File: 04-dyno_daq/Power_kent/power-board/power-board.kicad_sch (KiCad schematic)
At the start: 0 parts

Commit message: done with inputs, working on power conversion
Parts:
- added C1: 100uF, symbol Device:C
- added C2: 1uF, symbol Device:C
- added D1: D_TVS, symbol Device:D_TVS
- added F1: Polyfuse, symbol Device:Polyfuse
- added J1: USB_C_Receptacle_PowerOnly_24P, symbol Connector:USB_C_Receptacle_PowerOnly_24P
- added J2_(placeholder): Conn_01x02, symbol Connector_Generic:Conn_01x02
- added R1, R2: 5.1k, 10%, symbol Device:R
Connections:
- new net: C1.2, C2.2, F1.1, J1.A4 (VBUS), J1.A9 (VBUS), J1.B4 (VBUS), J1.B9 (VBUS)
- new net: J1.A5 (CC1), R1.1
- new net: J1.B5 (CC2), R2.1
- new net GND: C1.1, C2.1, D1.1 (A1), J1.A1 (GND), J1.A12 (GND), J1.B1 (GND), J1.B12 (GND), J1.SH (SHIELD), J2_(placeholder).2 (Pin_2), R1.2, R2.2
- new net VBAT: J2_(placeholder).1 (Pin_1)
- new net VBUS_PROT: D1.2 (A2), F1.2
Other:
- note added: "Battery Input"
- note added: "Power Conversion"
- note added: "USB C Input"

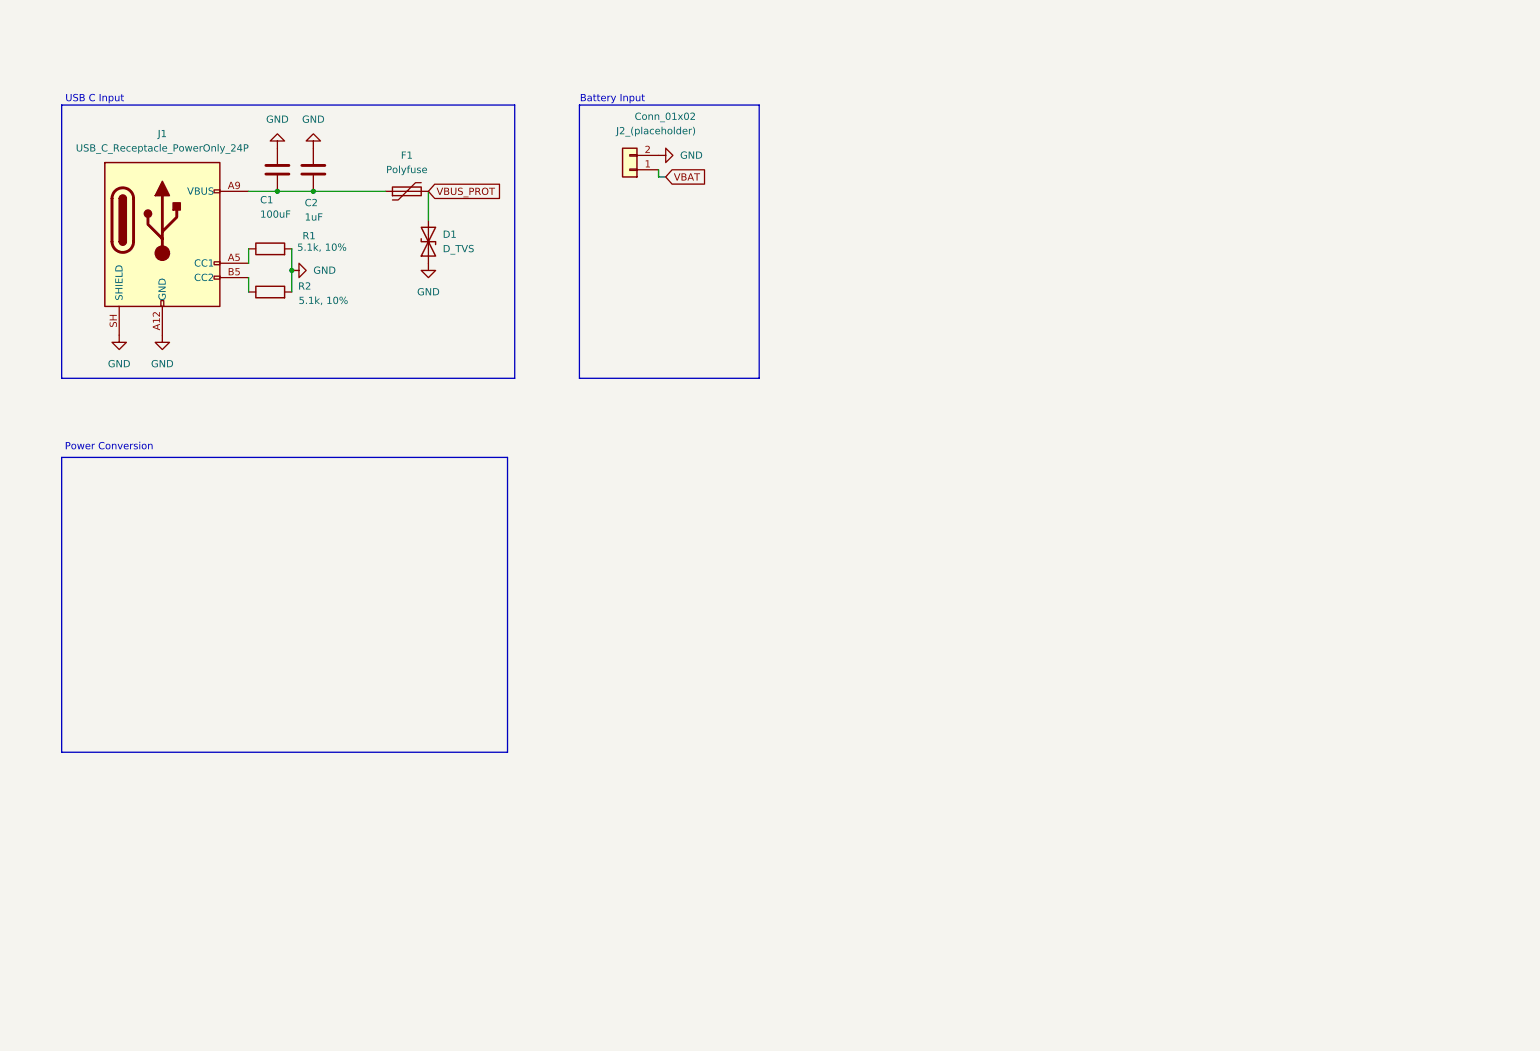
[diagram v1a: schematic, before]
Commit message: finished 1st version of schematic
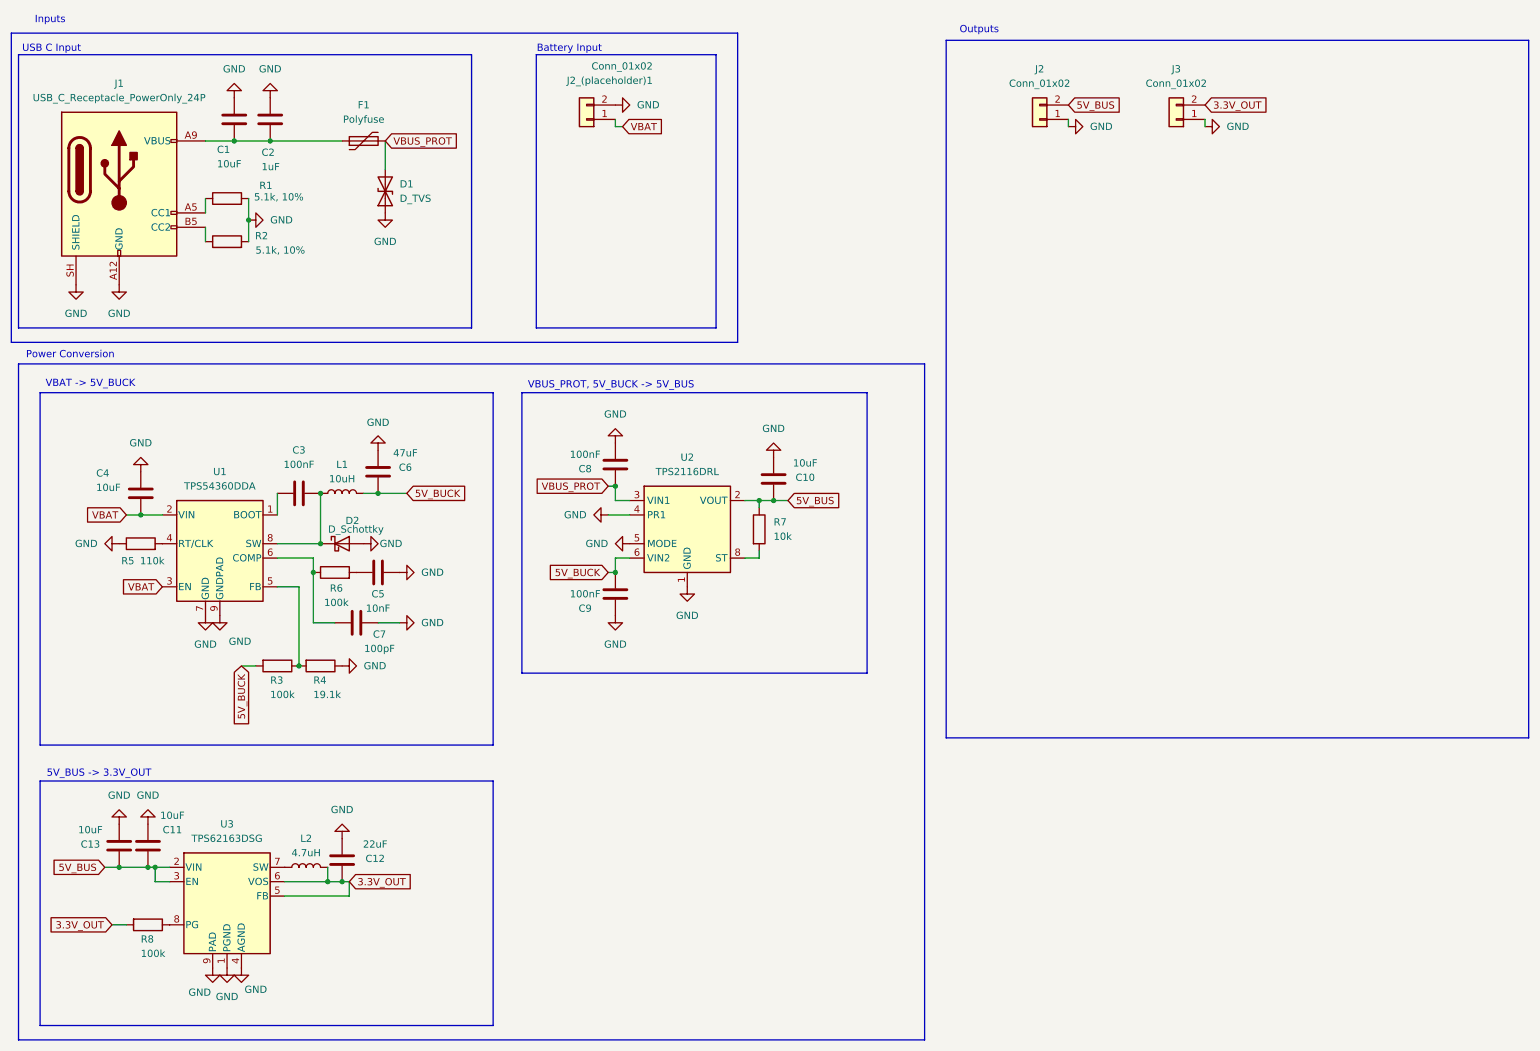
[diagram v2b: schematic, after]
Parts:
- added C10, C11, C13, C4: 10uF, symbol Device:C
- added C12: 22uF, symbol Device:C
- added C3, C8, C9: 100nF, symbol Device:C
- added C5: 10nF, symbol Device:C
- added C6: 47uF, symbol Device:C
- added C7: 100pF, symbol Device:C
- added D2: D_Schottky, symbol Device:D_Schottky
- added J2, J3: Conn_01x02, symbol Connector_Generic:Conn_01x02
- added L1: 10uH, symbol Device:L
- added L2: 4.7uH, symbol Device:L
- added R3, R6, R8: 100k, symbol Device:R
- added R4: 19.1k, symbol Device:R
- added R5: 110k, symbol Device:R
- added R7: 10k, symbol Device:R
- added U1: TPS54360DDA, Package_SO:TI_SO-PowerPAD-8_ThermalVias, symbol Regulator_Switching:TPS54360DDA
- added U2: TPS2116DRL, Package_TO_SOT_SMD:SOT-583-8, symbol Power_Management:TPS2116DRL
- added U3: TPS62163DSG, Package_SON:WSON-8-1EP_2x2mm_P0.5mm_EP0.9x1.6mm_ThermalVias, symbol Regulator_Switching:TPS62163DSG
- C1: value 100uF -> 10uF
- renumbered J2_(placeholder) to J2_(placeholder)1
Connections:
- net GND: now also C10.2, C11.2, C12.2, C13.2, C4.2, C5.2, C6.2, C7.2, C8.2, C9.1, D2.2 (A), J2.1 (Pin_1), J3.1 (Pin_1), R4.1, R5.1, U1.7 (GND), U1.9 (GNDPAD), U2.1 (GND), U2.4 (PR1), U2.5 (MODE), U3.1 (PGND), U3.4 (AGND), U3.9 (PAD)
- net VBAT: now also C4.1, U1.2 (VIN), U1.3 (EN)
- net VBUS_PROT: now also C8.1, U2.3 (VIN1)
- new net: C3.2, D2.1 (K), L1.1, U1.8 (SW)
- new net: C7.1, R6.1, U1.6 (COMP)
- new net: C5.1, R6.2
- new net: R8.1, U3.8 (PG)
- new net: R5.2, U1.4 (RT/CLK)
- new net: R7.2, U2.8 (ST)
- new net: L2.1, U3.7 (SW)
- new net: C3.1, U1.1 (BOOT)
- new net: R3.1, R4.2, U1.5 (FB)
- new net 3.3V_OUT: C12.1, J3.2 (Pin_2), L2.2, R8.2, U3.5 (FB), U3.6 (VOS)
- new net 5V_BUCK: C6.1, C9.2, L1.2, R3.2, U2.6 (VIN2)
- new net 5V_BUS: C10.1, C11.1, C13.1, J2.2 (Pin_2), R7.1, U2.2 (VOUT), U2.7 (VOUT), U3.2 (VIN), U3.3 (EN)
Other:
- note added: "5V_BUS -> 3.3V_OUT"
- note added: "Inputs"
- note added: "Outputs"
- note added: "VBAT -> 5V_BUCK"
- note added: "VBUS_PROT, 5V_BUCK -> 5V_BUS"
- moved on the sheet: C1, C2, D1, F1, J1, J2_(placeholder)1, R1, R2
